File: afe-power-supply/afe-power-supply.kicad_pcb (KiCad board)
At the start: 2 copper layers, 78.5 x 50.9 mm, 14 parts, among them J1 Screw_Terminal_01x03, J2 Screw_Terminal_01x02, J3 Conn_01x01, U1 Generic_DIP24_Dual_Isolated_D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

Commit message: Added/fixed mounting holes
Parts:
- added REF**: MountingHole_3.2mm_M3, MountingHole:MountingHole_3.2mm_M3, F.Cu at (144.3, 18.4)
- added REF**: MountingHole_3.2mm_M3, MountingHole:MountingHole_3.2mm_M3, F.Cu at (77.8, 57.3)
- added REF**: MountingHole_3.2mm_M3, MountingHole:MountingHole_3.2mm_M3, F.Cu at (77.8, 18.4)
- added REF**: MountingHole_3.2mm_M3, MountingHole:MountingHole_3.2mm_M3, F.Cu at (144.3, 57.3)
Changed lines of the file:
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@@
   (net 10 "Net-(J3-Pad1)")
   (net 11 "Net-(R1-Pad1)")
+  (footprint "MountingHole:MountingHole_3.2mm_M3" (layer "F.Cu")
+    (at 144.35 18.35)
+    (descr "Mounting Hole 3.2mm, no annular, M3")
+    (tags "mounting hole 3.2mm no annular m3")
+    (attr exclude_from_pos_files exclude_from_bom)
+    (fp_text reference "REF**" (at 0 -4.2) (layer "F.SilkS") hide
+      (effects (font (size 1 1) (thickness 0.15)))
+    )
+    (fp_text value "MountingHole_3.2mm_M3" (at 0 4.2) (layer "F.Fab") hide
+      (effects (font (size 1 1) (thickness 0.15)))
+    )
+    (fp_text user "${REFERENCE}" (at 0 0) (layer "F.Fab")
+      (effects (font (size 1 1) (thickness 0.15)))
+    )
+    (fp_circle (center 0 0) (end 3.2 0) (layer "Cmts.User") (width 0.15) (fill none))
+    (fp_circle (center 0 0) (end 3.45 0) (layer "F.CrtYd") (width 0.05) (fill none))
+    (pad "" np_thru_hole circle (at 0 0) (size 3.2 3.2) (drill 3.2) (layers *.Cu *.Mask))
+  )
+  (footprint "MountingHole:MountingHole_3.2mm_M3" (layer "F.Cu")
+    (at 77.8 57.3)
+    (descr "Mounting Hole 3.2mm, no annular, M3")
+    (tags "mounting hole 3.2mm no annular m3")
+    (attr exclude_from_pos_files exclude_from_bom)
+    (fp_text reference "REF**" (at 0 -4.2) (layer "F.SilkS") hide
+      (effects (font (size 1 1) (thickness 0.15)))
+    )
+    (fp_text value "MountingHole_3.2mm_M3" (at 0 4.2) (layer "F.Fab") hide
+      (effects (font (size 1 1) (thickness 0.15)))
+    )
+    (fp_text user "${REFERENCE}" (at 0 0) (layer "F.Fab")
+      (effects (font (size 1 1) (thickness 0.15)))
+    )
+    (fp_circle (center 0 0) (end 3.2 0) (layer "Cmts.User") (width 0.15) (fill none))
+    (fp_circle (center 0 0) (end 3.45 0) (layer "F.CrtYd") (width 0.05) (fill none))
+    (pad "" np_thru_hole circle (at 0 0) (size 3.2 3.2) (drill 3.2) (layers *.Cu *.Mask))
+  )
+  (footprint "MountingHole:MountingHole_3.2mm_M3" (layer "F.Cu")
+    (at 77.8 18.35)
+    (descr "Mounting Hole 3.2mm, no annular, M3")
+    (tags "mounting hole 3.2mm no annular m3")
+    (attr exclude_from_pos_files exclude_from_bom)
+    (fp_text reference "REF**" (at 0 -4.2) (layer "F.SilkS") hide
+      (effects (font (size 1 1) (thickness 0.15)))
+    )
+    (fp_text value "MountingHole_3.2mm_M3" (at 0 4.2) (layer "F.Fab") hide
+      (effects (font (size 1 1) (thickness 0.15)))
+    )
+    (fp_text user "${REFERENCE}" (at 0 0) (layer "F.Fab")
+      (effects (font (size 1 1) (thickness 0.15)))
+    )
+    (fp_circle (center 0 0) (end 3.2 0) (layer "Cmts.User") (width 0.15) (fill none))
+    (fp_circle (center 0 0) (end 3.45 0) (layer "F.CrtYd") (width 0.05) (fill none))
+    (pad "" np_thru_hole circle (at 0 0) (size 3.2 3.2) (drill 3.2) (layers *.Cu *.Mask))
+  )
   (footprint "Capacitor_THT:CP_Radial_D16.0mm_P7.50mm" (layer "F.Cu")
     (at 94.537246 21.2)
@@
     )
   )
+  (footprint "MountingHole:MountingHole_3.2mm_M3" (layer "F.Cu")
+    (at 144.35 57.3)
+    (descr "Mounting Hole 3.2mm, no annular, M3")
+    (tags "mounting hole 3.2mm no annular m3")
+    (attr exclude_from_pos_files exclude_from_bom)
+    (fp_text reference "REF**" (at 0 -4.2) (layer "F.SilkS") hide
+      (effects (font (size 1 1) (thickness 0.15)))
+    )
+    (fp_text value "MountingHole_3.2mm_M3" (at 0 4.2) (layer "F.Fab") hide
+      (effects (font (size 1 1) (thickness 0.15)))
+    )
+    (fp_text user "${REFERENCE}" (at 0 0) (layer "F.Fab")
+      (effects (font (size 1 1) (thickness 0.15)))
+    )
+    (fp_circle (center 0 0) (end 3.2 0) (layer "Cmts.User") (width 0.15) (fill none))
+    (fp_circle (center 0 0) (end 3.45 0) (layer "F.CrtYd") (width 0.05) (fill none))
+    (pad "" np_thru_hole circle (at 0 0) (size 3.2 3.2) (drill 3.2) (layers *.Cu *.Mask))
+  )
   (footprint "LED_SMD:LED_0805_2012Metric_Pad1.15x1.40mm_HandSolder" (layer "F.Cu")

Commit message: Updated boards with dates, silk, mounting holes
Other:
- board text added: "AFE meas. supply v1.0 - 08.2022"
- board text removed: "AFE meas. supply v1.0 - 07.2022"
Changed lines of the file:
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@@
     (effects (font (size 0.8 0.8) (thickness 0.2)))
   )
-  (gr_text "AFE meas. supply\nv1.0 - 07.2022" (at 72.5 14.2) (layer "F.SilkS")
+  (gr_text "AFE meas. supply\nv1.0 - 08.2022" (at 122.047 59.8424) (layer "F.SilkS")
     (effects (font (size 0.8 0.8) (thickness 0.2)) (justify left))
   )

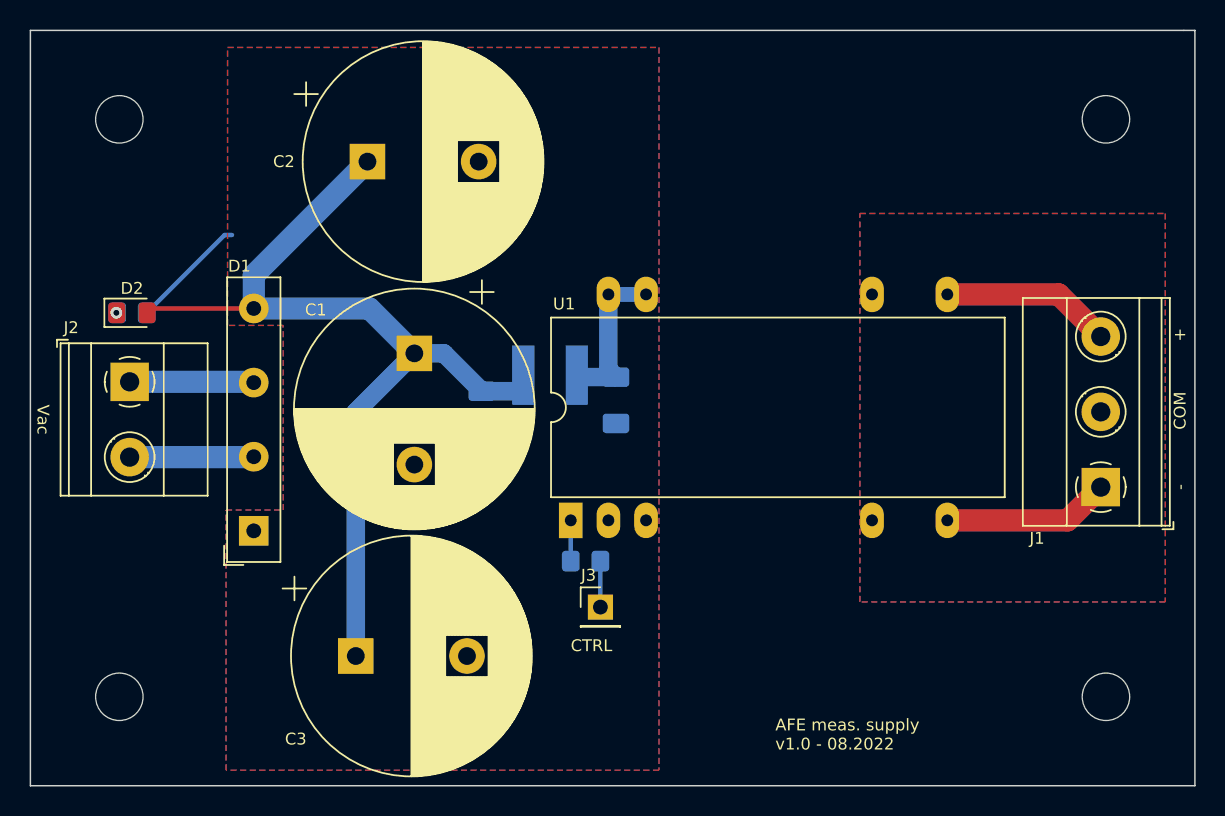
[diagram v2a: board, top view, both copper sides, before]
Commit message: Added fuse and generated gerber files for afe power supply
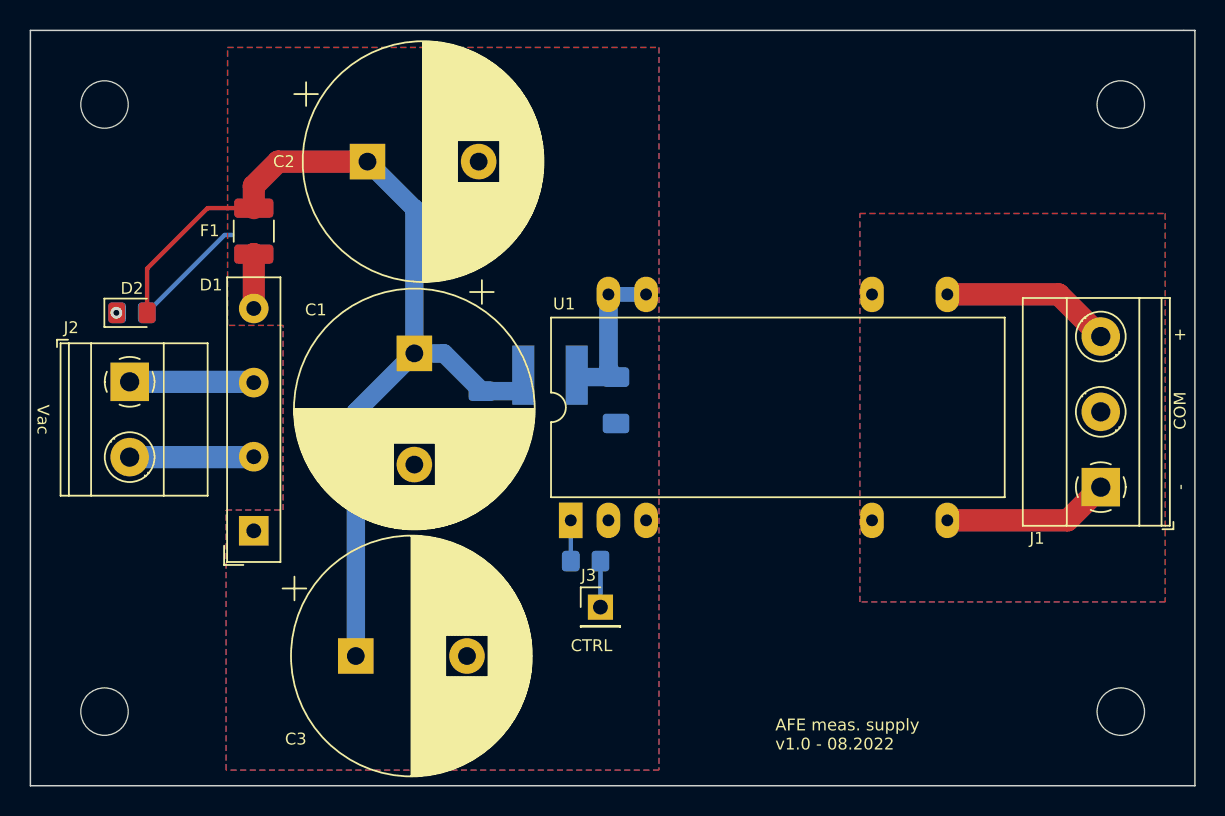
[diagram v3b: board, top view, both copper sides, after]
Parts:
- removed the REF** at (144.3, 18.4)
- removed the REF** at (77.8, 57.3)
- removed the REF** at (77.8, 18.4)
- removed the REF** at (144.3, 57.3)
- added F1: Polyfuse, Resistor_SMD:R_1210_3225Metric_Pad1.30x2.65mm_HandSolder, F.Cu at (86.9, 25.9)
- added REF**: MountingHole_3.2mm_M3, MountingHole:MountingHole_3.2mm_M3, F.Cu at (76.8, 17.4)
- added REF**: MountingHole_3.2mm_M3, MountingHole:MountingHole_3.2mm_M3, F.Cu at (145.3, 17.4)
- added REF**: MountingHole_3.2mm_M3, MountingHole:MountingHole_3.2mm_M3, F.Cu at (145.3, 58.3)
- added REF**: MountingHole_3.2mm_M3, MountingHole:MountingHole_3.2mm_M3, F.Cu at (76.8, 58.3)
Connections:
- D1 pad 4: /V_DC_+ -> Net-(D1-Pad4)
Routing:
- net Net-(D1-Pad4): track 0.00 -> 3.67 mm
- net /V_DC_+: track 64.0 -> 67.5 mm
